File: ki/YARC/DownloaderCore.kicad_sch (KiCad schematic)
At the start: 13 parts, among them J1 NANOIO_EXT, J2 MCR_EXT, J3 PULSE_EXT, U1 74HCT574, U2 74HCT574, U3 74HCT574, U4 74HCT574, U5 74HCT574, U6 74LS138, U7 74HCT574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

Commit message: Partway through Nano-specific optimizations to ard/port_task.h
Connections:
- net VCC: no longer U4.1 (OE)
- net ~{DATA_LOW_EN}: now also U4.1 (OE)
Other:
- note added: "MCR 0, 1, 2, 7"
- note added: "MCR4 YARC FASTCLKEN#"
- note added: "MCR5 YARC/NANO#"
- note added: "MCR6 SVC STATUS"
- note added: "NOT USED"
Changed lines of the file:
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@@
   (junction (at 149.86 152.4) (diameter 0) (color 0 0 0 0)
   )
-  (junction (at 43.18 55.88) (diameter 0) (color 0 0 0 0)
-  )
   (junction (at 165.1 147.32) (diameter 0) (color 0 0 0 0)
   )
@@
     (stroke (width 0) (type default) (color 0 0 0 0))
   )
-  (wire (pts (xy 76.2 55.88) (xy 43.18 55.88))
-    (stroke (width 0) (type default) (color 0 0 0 0))
-  )
   (wire (pts (xy 160.02 157.48) (xy 160.02 147.32))
     (stroke (width 0) (type default) (color 0 0 0 0))
@@
     (stroke (width 0) (type default) (color 0 0 0 0))
   )
-  (wire (pts (xy 76.2 53.34) (xy 76.2 55.88))
-    (stroke (width 0) (type default) (color 0 0 0 0))
-  )
   (bus (pts (xy 73.66 177.8) (xy 73.66 185.42))
     (stroke (width 0) (type default) (color 0 0 0 0))
@@
     (stroke (width 0) (type default) (color 0 0 0 0))
   )
-  (wire (pts (xy 43.18 55.88) (xy 43.18 58.42))
+  (wire (pts (xy 43.18 50.8) (xy 43.18 58.42))
     (stroke (width 0) (type default) (color 0 0 0 0))
   )
@@
     (stroke (width 0) (type default) (color 0 0 0 0))
   )
-  (wire (pts (xy 43.18 50.8) (xy 43.18 55.88))
-    (stroke (width 0) (type default) (color 0 0 0 0))
-  )
   (bus (pts (xy 127 15.24) (xy 129.54 15.24))
     (stroke (width 0) (type default) (color 0 0 0 0))
@@
     (stroke (width 0) (type default) (color 0 0 0 0))
   )
+  (wire (pts (xy 76.2 53.34) (xy 72.39 53.34))
+    (stroke (width 0) (type default) (color 0 0 0 0))
+  )
   (wire (pts (xy 124.46 152.4) (xy 149.86 152.4))
     (stroke (width 0) (type default) (color 0 0 0 0))
@@
     (stroke (width 0) (type default) (color 0 0 0 0))
   )
-  (text "MCR3,6 not bussed" (at 241.3 43.18 0)
+  (text "MCR3,6 not bussed" (at 234.95 49.53 0)
+    (effects (font (size 1.27 1.27)) (justify left bottom))
+  )
+  (text "MCR 0, 1, 2, 7" (at 238.76 101.6 0)
+    (effects (font (size 1.27 1.27)) (justify left bottom))
+  )
+  (text "NOT USED" (at 238.76 104.14 0)
+    (effects (font (size 1.27 1.27)) (justify left bottom))
+  )
+  (text "MCR5 YARC/NANO#" (at 233.68 87.63 0)
+    (effects (font (size 1.27 1.27)) (justify left bottom))
+  )
+  (text "MCR6 SVC STATUS\n" (at 237.49 80.01 0)
+    (effects (font (size 1.27 1.27)) (justify left bottom))
+  )
+  (text "MCR4 YARC FASTCLKEN#" (at 233.68 90.17 0)
     (effects (font (size 1.27 1.27)) (justify left bottom))
   )
@@
     )
   )
+  (global_label "~{DATA_LOW_EN}" (shape input) (at 72.39 53.34 180) (fields_autoplaced)
+    (effects (font (size 1.27 1.27)) (justify right))
+    (property "Intersheet References" "${INTERSHEET_REFS}" (id 0) (at 57.3374 53.2606 0)
+      (effects (font (size 1.27 1.27)) (justify right) hide)
+    )
+  )

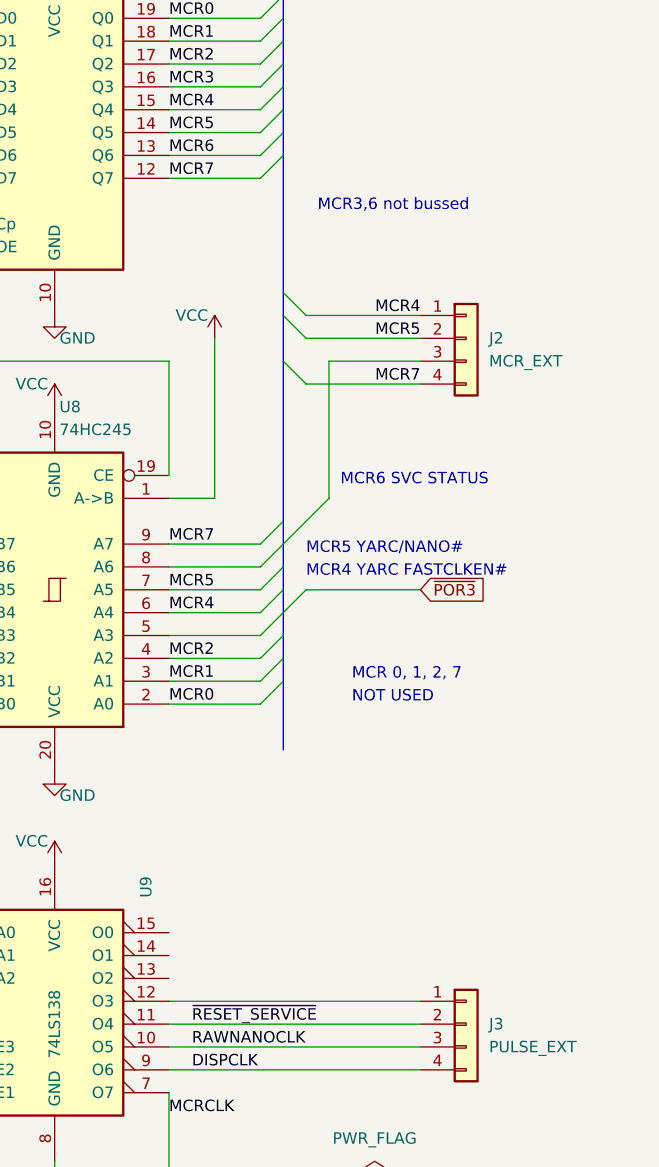
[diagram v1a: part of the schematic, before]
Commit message: Adding microcode control lines from Nano
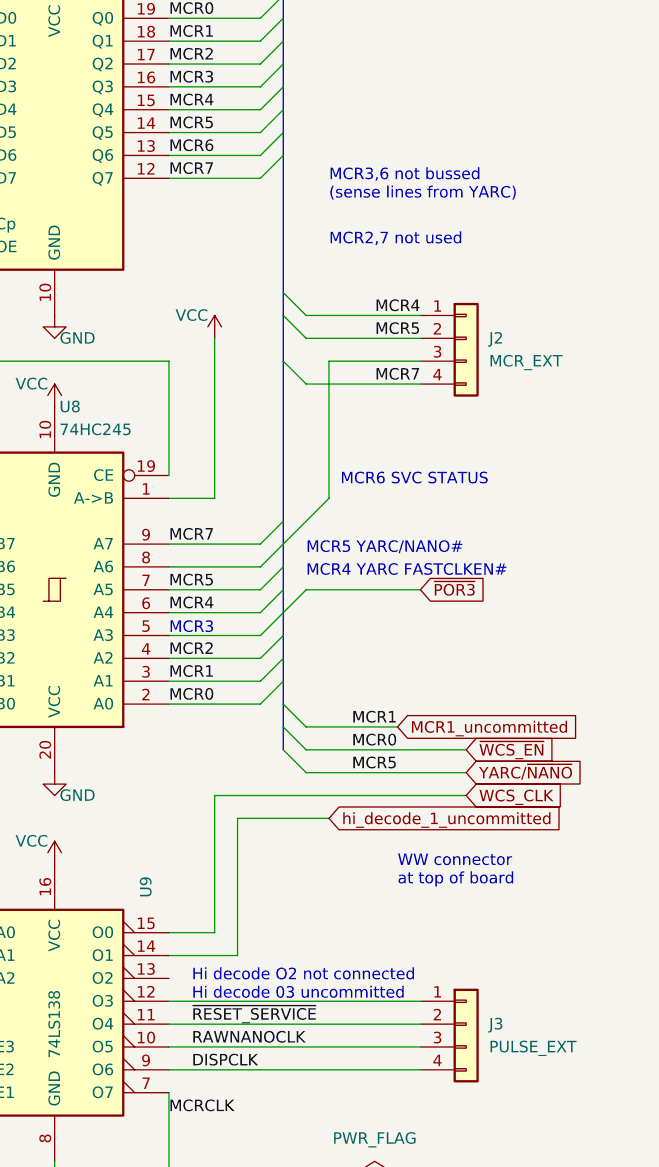
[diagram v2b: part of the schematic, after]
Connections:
- net MCR5 is gone; now on net YARC/~{NANO}: J2.2 (Pin_2), U7.14 (Q5), U8.7 (A5)
- net hi_decode_1_uncommitted: now reaches U9.14 (O1)
- net WCS_CLK: now reaches U9.15 (O0)
- net MCR0 renamed ~{WCS_EN}
- net MCR1 renamed MCR1_uncommitted
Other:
- note added: "Hi decode O2 not connected Hi decode 03 uncommitted"
- note added: "MCR2,7 not used"
- note added: "MCR3"
- note added: "MCR3,6 not bussed (sense lines from YARC)"
- note added: "WW connector at top of board"
- note removed: "MCR 0, 1, 2, 7"
- note removed: "MCR3,6 not bussed"
- note removed: "NOT USED"
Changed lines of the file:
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@@
+    (stroke (width 0) (type default) (color 0 0 0 0))
+  )
+  (bus_entry (at 231.14 109.22) (size 2.54 2.54)
     (stroke (width 0) (type default) (color 0 0 0 0))
   )
@@
     (stroke (width 0) (type default) (color 0 0 0 0))
   )
+  (bus_entry (at 231.14 106.68) (size 2.54 2.54)
+    (stroke (width 0) (type default) (color 0 0 0 0))
+  )
   (bus_entry (at 93.98 63.5) (size 2.54 -2.54)
     (stroke (width 0) (type default) (color 0 0 0 0))
@@
     (stroke (width 0) (type default) (color 0 0 0 0))
   )
+  (bus_entry (at 231.14 104.14) (size 2.54 2.54)
+    (stroke (width 0) (type default) (color 0 0 0 0))
+  )
   (bus_entry (at 73.66 160.02) (size -2.54 2.54)
     (stroke (width 0) (type default) (color 0 0 0 0))
@@
     (stroke (width 0) (type default) (color 0 0 0 0))
   )
+  (wire (pts (xy 226.06 132.08) (xy 226.06 116.84))
+    (stroke (width 0) (type default) (color 0 0 0 0))
+  )
   (wire (pts (xy 17.78 81.28) (xy 30.48 81.28))
     (stroke (width 0) (type default) (color 0 0 0 0))
@@
     (stroke (width 0) (type default) (color 0 0 0 0))
   )
+  (wire (pts (xy 233.68 106.68) (xy 243.84 106.68))
+    (stroke (width 0) (type default) (color 0 0 0 0))
+  )
   (bus (pts (xy 15.24 73.66) (xy 15.24 76.2))
     (stroke (width 0) (type default) (color 0 0 0 0))
@@
     (stroke (width 0) (type default) (color 0 0 0 0))
   )
+  (wire (pts (xy 226.06 116.84) (xy 236.22 116.84))
+    (stroke (width 0) (type default) (color 0 0 0 0))
+  )
   (wire (pts (xy 124.46 149.86) (xy 147.32 149.86))
     (stroke (width 0) (type default) (color 0 0 0 0))
@@
     (stroke (width 0) (type default) (color 0 0 0 0))
   )
+  (wire (pts (xy 251.46 114.3) (xy 223.52 114.3))
+    (stroke (width 0) (type default) (color 0 0 0 0))
+  )
   (wire (pts (xy 223.52 81.28) (xy 223.52 63.5))
     (stroke (width 0) (type default) (color 0 0 0 0))
@@
     (stroke (width 0) (type default) (color 0 0 0 0))
   )
+  (bus (pts (xy 231.14 104.14) (xy 231.14 106.68))
+    (stroke (width 0) (type default) (color 0 0 0 0))
+  )
   (wire (pts (xy 17.78 129.54) (xy 30.48 129.54))
     (stroke (width 0) (type default) (color 0 0 0 0))
@@
     (stroke (width 0) (type default) (color 0 0 0 0))
   )
-  (bus (pts (xy 231.14 101.6) (xy 231.14 109.22))
+  (bus (pts (xy 231.14 101.6) (xy 231.14 104.14))
     (stroke (width 0) (type default) (color 0 0 0 0))
   )
@@
     (stroke (width 0) (type default) (color 0 0 0 0))
   )
+  (bus (pts (xy 231.14 106.68) (xy 231.14 109.22))
+    (stroke (width 0) (type default) (color 0 0 0 0))
+  )
   (wire (pts (xy 193.04 134.62) (xy 182.88 134.62))
     (stroke (width 0) (type default) (color 0 0 0 0))
@@
     (stroke (width 0) (type default) (color 0 0 0 0))
   )
+  (wire (pts (xy 233.68 111.76) (xy 251.46 111.76))
+    (stroke (width 0) (type default) (color 0 0 0 0))
+  )
   (bus (pts (xy 15.24 114.3) (xy 15.24 116.84))
     (stroke (width 0) (type default) (color 0 0 0 0))
@@
     (stroke (width 0) (type default) (color 0 0 0 0))
   )
+  (wire (pts (xy 218.44 132.08) (xy 226.06 132.08))
+    (stroke (width 0) (type default) (color 0 0 0 0))
+  )
   (wire (pts (xy 218.44 81.28) (xy 223.52 81.28))
     (stroke (width 0) (type default) (color 0 0 0 0))
@@
     (stroke (width 0) (type default) (color 0 0 0 0))
   )
+  (wire (pts (xy 223.52 114.3) (xy 223.52 129.54))
+    (stroke (width 0) (type default) (color 0 0 0 0))
+  )
   (wire (pts (xy 91.44 60.96) (xy 91.44 53.34))
     (stroke (width 0) (type default) (color 0 0 0 0))
@@
     (stroke (width 0) (type default) (color 0 0 0 0))
   )
+  (wire (pts (xy 233.68 109.22) (xy 251.46 109.22))
+    (stroke (width 0) (type default) (color 0 0 0 0))
+  )
   (wire (pts (xy 193.04 129.54) (xy 177.8 129.54))
     (stroke (width 0) (type default) (color 0 0 0 0))
@@
     (stroke (width 0) (type default) (color 0 0 0 0))
   )
+  (wire (pts (xy 223.52 129.54) (xy 218.44 129.54))
+    (stroke (width 0) (type default) (color 0 0 0 0))
+  )
   (bus (pts (xy 73.66 116.84) (xy 73.66 119.38))
     (stroke (width 0) (type default) (color 0 0 0 0))
@@
     (stroke (width 0) (type default) (color 0 0 0 0))
   )
-  (text "MCR3,6 not bussed" (at 234.95 49.53 0)
-    (effects (font (size 1.27 1.27)) (justify left bottom))
-  )
-  (text "MCR 0, 1, 2, 7" (at 238.76 101.6 0)
-    (effects (font (size 1.27 1.27)) (justify left bottom))
-  )
-  (text "NOT USED" (at 238.76 104.14 0)
+  (text "MCR3,6 not bussed\n(sense lines from YARC)" (at 236.22 48.26 0)
+    (effects (font (size 1.27 1.27)) (justify left bottom))
+  )
+  (text "Hi decode O2 not connected\nHi decode 03 uncommitted"
+    (at 220.98 137.16 0)
     (effects (font (size 1.27 1.27)) (justify left bottom))
   )
@@
     (effects (font (size 1.27 1.27)) (justify left bottom))
   )
+  (text "MCR3" (at 218.44 96.52 0)
+    (effects (font (size 1.27 1.27)) (justify left bottom))
+  )
+  (text "WW connector\nat top of board" (at 243.84 124.46 0)
+    (effects (font (size 1.27 1.27)) (justify left bottom))
+  )
+  (text "MCR2,7 not used" (at 236.22 53.34 0)
+    (effects (font (size 1.27 1.27)) (justify left bottom))
+  )
   (label "NANOIO7" (at 177.8 86.36 0)
     (effects (font (size 1.27 1.27)) (justify left bottom))
   )
+  (label "MCR1" (at 238.76 106.68 0)
+    (effects (font (size 1.27 1.27)) (justify left bottom))
+  )
   (label "NANOIO7" (at 83.82 60.96 90)
     (effects (font (size 1.27 1.27)) (justify left bottom))
@@
     (effects (font (size 1.27 1.27)) (justify left bottom))
   )
+  (label "MCR5" (at 238.76 111.76 0)
+    (effects (font (size 1.27 1.27)) (justify left bottom))
+  )
   (label "NANOIO4" (at 55.88 76.2 0)
     (effects (font (size 1.27 1.27)) (justify left bottom))
@@
     (effects (font (size 1.27 1.27)) (justify right bottom))
   )
+  (label "MCR0" (at 238.76 109.22 0)
+    (effects (font (size 1.27 1.27)) (justify left bottom))
+  )
   (label "NANOIO5" (at 134.62 60.96 90)
     (effects (font (size 1.27 1.27)) (justify left bottom))
@@
   (label "NANOIO4" (at 177.8 38.1 0)
     (effects (font (size 1.27 1.27)) (justify left bottom))
+  )
+  (global_label "WCS_CLK" (shape input) (at 251.46 114.3 0) (fields_autoplaced)
+    (effects (font (size 1.27 1.27)) (justify left))
+    (property "Intersheet References" "${INTERSHEET_REFS}" (id 0) (at 262.3398 114.2206 0)
+      (effects (font (size 1.27 1.27)) (justify left) hide)
+    )
   )
   (global_label "~{POR3}" (shape input) (at 246.38 91.44 0) (fields_autoplaced)
@@
     )
   )
+  (global_label "YARC{slash}~{NANO}" (shape input) (at 251.46 111.76 0) (fields_autoplaced)
+    (effects (font (size 1.27 1.27)) (justify left))
+    (property "Intersheet References" "${INTERSHEET_REFS}" (id 0) (at 265.0007 111.6806 0)
+      (effects (font (size 1.27 1.27)) (justify left) hide)
+    )
+  )
+  (global_label "~{WCS_EN}" (shape input) (at 251.46 109.22 0) (fields_autoplaced)
+    (effects (font (size 1.27 1.27)) (justify left))
+    (property "Intersheet References" "${INTERSHEET_REFS}" (id 0) (at 261.2512 109.1406 0)
+      (effects (font (size 1.27 1.27)) (justify left) hide)
+    )
+  )
   (global_label "SYSCLK7" (shape input) (at 27.94 185.42 180) (fields_autoplaced)
     (effects (font (size 1.27 1.27)) (justify right))
@@
       (effects (font (size 1.27 1.27)) (justify left) hide)
     )
+  )
+  (global_label "hi_decode_1_uncommitted" (shape input) (at 236.22 116.84 0) (fields_autoplaced)
+    (effects (font (size 1.27 1.27)) (justify left))
+    (property "Intersheet References" "${INTERSHEET_REFS}" (id 0) (at 263.4283 116.7606 0)
+      (effects (font (size 1.27 1.27)) (justify left) hide)
+    )
+  )
+  (global_label "MCR1_uncommitted" (shape input) (at 243.84 106.68 0) (fields_autoplaced)
+    (effects (font (size 1.27 1.27)) (justify left))
+    (property "Intersheet References" "${INTERSHEET_REFS}" (id 0) (at 264.6379 106.6006 0)
+      (effects (font (size 1.27 1.27)) (justify left) hide)
+    )

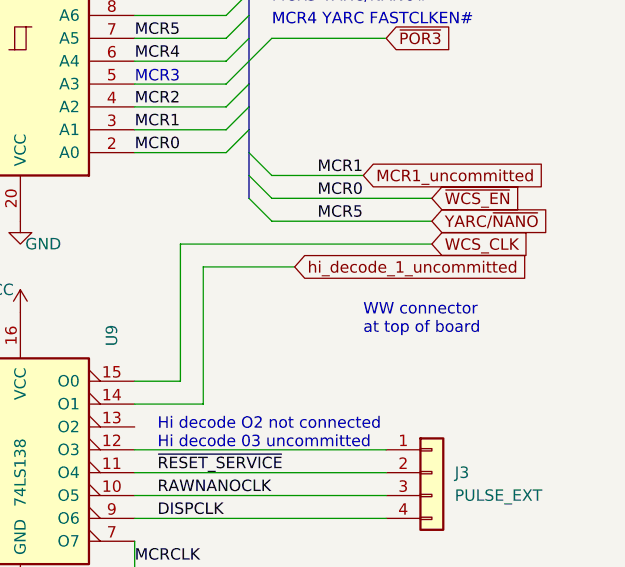
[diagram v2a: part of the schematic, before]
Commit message: Nano IR clock and mem enable changes documented in Ki, Ftz, and port_task.h
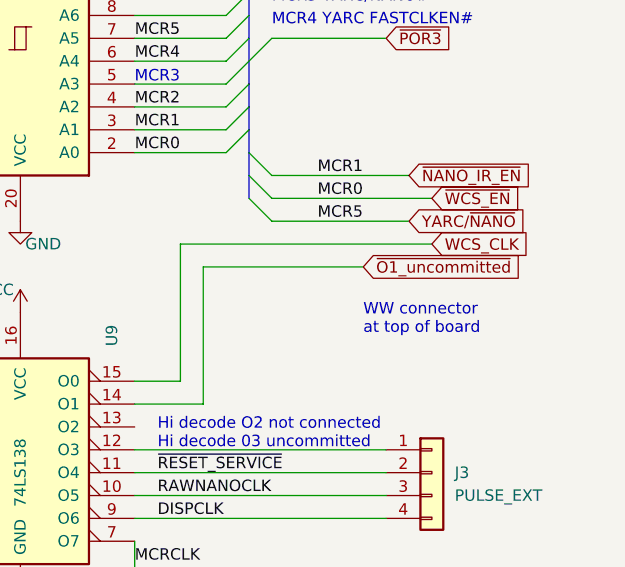
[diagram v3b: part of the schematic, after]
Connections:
- net MCR1_uncommitted renamed ~{NANO_IR_EN}
- net hi_decode_1_uncommitted renamed ~{O1_uncommitted}
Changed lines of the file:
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@@
+    (stroke (width 0) (type default) (color 0 0 0 0))
+  )
+  (wire (pts (xy 226.06 116.84) (xy 226.06 132.08))
     (stroke (width 0) (type default) (color 0 0 0 0))
   )
@@
     (stroke (width 0) (type default) (color 0 0 0 0))
   )
-  (wire (pts (xy 226.06 132.08) (xy 226.06 116.84))
-    (stroke (width 0) (type default) (color 0 0 0 0))
-  )
   (wire (pts (xy 17.78 81.28) (xy 30.48 81.28))
     (stroke (width 0) (type default) (color 0 0 0 0))
@@
     (stroke (width 0) (type default) (color 0 0 0 0))
   )
-  (wire (pts (xy 233.68 106.68) (xy 243.84 106.68))
+  (wire (pts (xy 233.68 106.68) (xy 248.92 106.68))
     (stroke (width 0) (type default) (color 0 0 0 0))
   )
@@
     (stroke (width 0) (type default) (color 0 0 0 0))
   )
-  (wire (pts (xy 226.06 116.84) (xy 236.22 116.84))
-    (stroke (width 0) (type default) (color 0 0 0 0))
-  )
   (wire (pts (xy 124.46 149.86) (xy 147.32 149.86))
     (stroke (width 0) (type default) (color 0 0 0 0))
@@
     (stroke (width 0) (type default) (color 0 0 0 0))
   )
+  (wire (pts (xy 243.84 116.84) (xy 226.06 116.84))
+    (stroke (width 0) (type default) (color 0 0 0 0))
+  )
   (wire (pts (xy 71.12 124.46) (xy 55.88 124.46))
     (stroke (width 0) (type default) (color 0 0 0 0))
@@
     (stroke (width 0) (type default) (color 0 0 0 0))
   )
-  (wire (pts (xy 233.68 111.76) (xy 251.46 111.76))
+  (wire (pts (xy 233.68 111.76) (xy 248.92 111.76))
     (stroke (width 0) (type default) (color 0 0 0 0))
   )
@@
     )
   )
-  (global_label "YARC{slash}~{NANO}" (shape input) (at 251.46 111.76 0) (fields_autoplaced)
+  (global_label "~{O1_uncommitted}" (shape input) (at 243.84 116.84 0) (fields_autoplaced)
     (effects (font (size 1.27 1.27)) (justify left))
-    (property "Intersheet References" "${INTERSHEET_REFS}" (id 0) (at 265.0007 111.6806 0)
+    (property "Intersheet References" "${INTERSHEET_REFS}" (id 0) (at 261.9769 116.7606 0)
+      (effects (font (size 1.27 1.27)) (justify left) hide)
+    )
+  )
+  (global_label "YARC{slash}~{NANO}" (shape input) (at 248.92 111.76 0) (fields_autoplaced)
+    (effects (font (size 1.27 1.27)) (justify left))
+    (property "Intersheet References" "${INTERSHEET_REFS}" (id 0) (at 262.4607 111.6806 0)
       (effects (font (size 1.27 1.27)) (justify left) hide)
     )
@@
     )
   )
-  (global_label "hi_decode_1_uncommitted" (shape input) (at 236.22 116.84 0) (fields_autoplaced)
+  (global_label "~{NANO_IR_EN}" (shape input) (at 248.92 106.68 0) (fields_autoplaced)
     (effects (font (size 1.27 1.27)) (justify left))
-    (property "Intersheet References" "${INTERSHEET_REFS}" (id 0) (at 263.4283 116.7606 0)
+    (property "Intersheet References" "${INTERSHEET_REFS}" (id 0) (at 262.7026 106.6006 0)
       (effects (font (size 1.27 1.27)) (justify left) hide)
     )
-  )
-  (global_label "MCR1_uncommitted" (shape input) (at 243.84 106.68 0) (fields_autoplaced)
-    (effects (font (size 1.27 1.27)) (justify left))
-    (property "Intersheet References" "${INTERSHEET_REFS}" (id 0) (at 264.6379 106.6006 0)
-      (effects (font (size 1.27 1.27)) (justify left) hide)
-    )
